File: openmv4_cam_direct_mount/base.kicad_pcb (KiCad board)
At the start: 4 copper layers, 35.6 x 44.5 mm, 59 parts, among them M1 9774030243R, M2 9774030243R, Q1 BSS138, Q2 Si2301BDS, U1 STM32H743VIT6, U5 TPS731XX, U8 PAM2305AABADJ, X1 MF-CON-MICROUSB-RIGHT, X2 USD-1040310811, X3 DF12-36-DS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

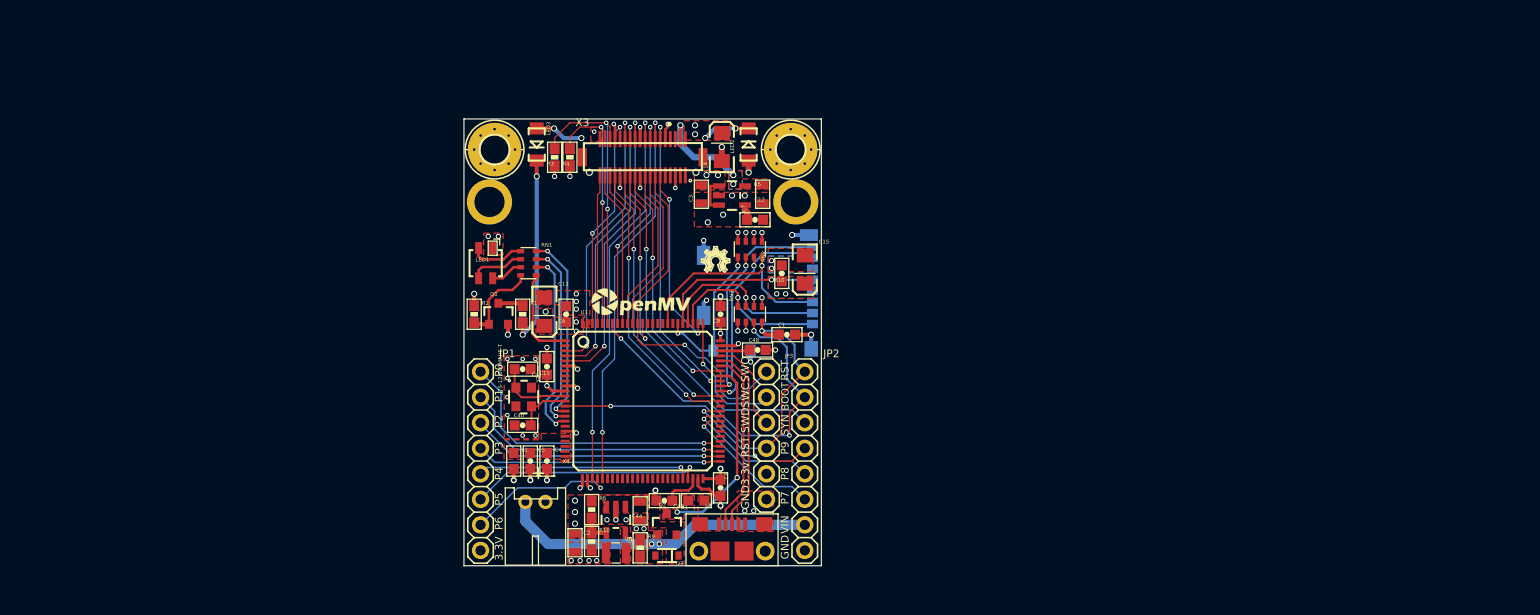
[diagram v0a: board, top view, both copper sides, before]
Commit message: Fixed camera mount hole links
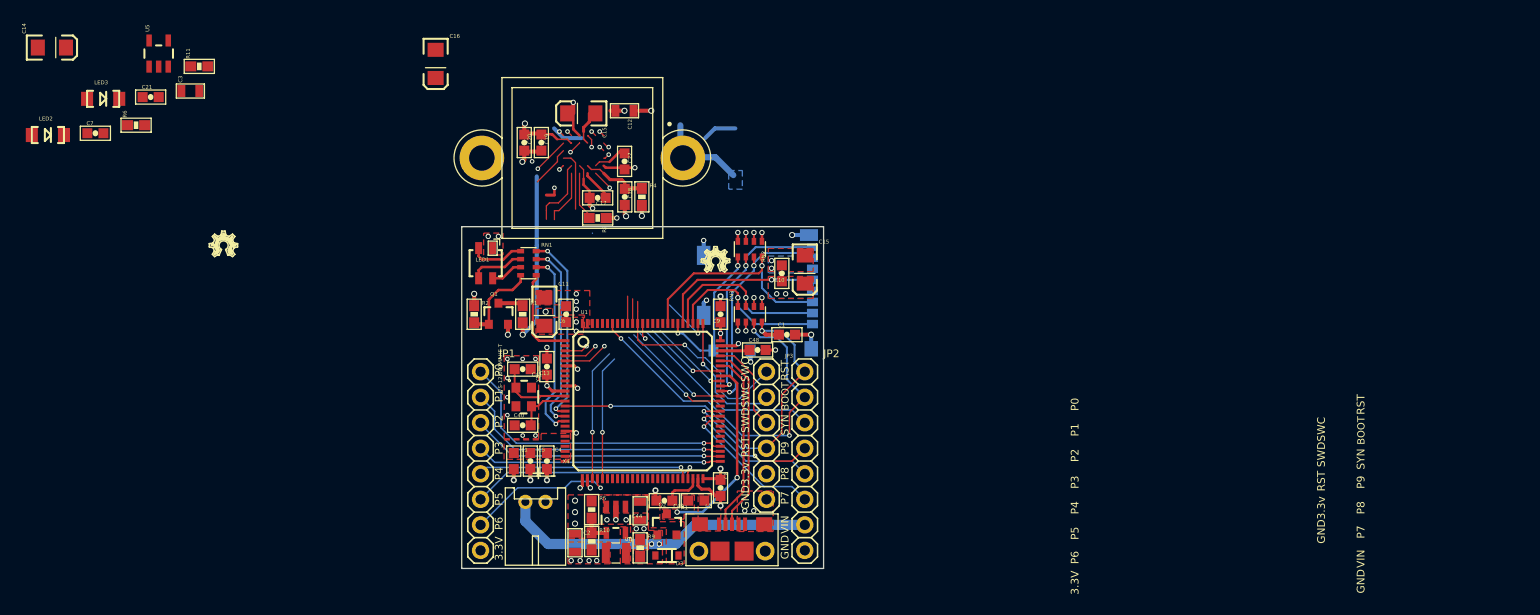
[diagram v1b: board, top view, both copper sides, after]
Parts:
- removed H1, H2: MOUNT-PAD-ROUND2.8, base:2,8-PAD
- removed M1, M2: 9774030243R, base:9774030151R
- removed U$1: , base:WEEE
- removed U$2: , base:ROHS
- removed U$4: , base:OMV-LOGO-SMALL
- removed X3: DF12-36-DS, base:DF12-36-DS
- added C15: 47uF, base:EIA3216, F.Cu at (142.4, 82.2)
- added C16: 47uF, base:EIA3216, F.Cu at (127.9, 77.3)
- added C17: 0.1uF, base:0603-CAP, F.Cu at (144.0, 90.6)
- added C18: 22uF, base:0603-CAP, F.Cu at (146.7, 90.5)
- added C19: 4.7uF, base:0603-CAP, F.Cu at (138.4, 85.1)
- added C20: 0.1uF, base:0603-CAP, F.Cu at (136.7, 85.1)
- added C21: 0.1uF, base:0603-CAP, F.Cu at (99.5, 80.6)
- added C22: 0.1uF, base:0603-CAP, F.Cu at (146.7, 87.0)
- added LM1: LENSMOUNT20MM, openmv3:LENSMOUNT-20MM, F.Cu at (142.5, 86.7)
- added LOGO1: OSHW_LOGO_FILLX0100-NT, base:OSHW_FILLX100_NOTEXT, F.Cu at (105.4, 96.5)
- added R11: 10K, base:0603-RES, F.Cu at (104.4, 77.5)
- added R6: 10K, base:0603-RES, F.Cu at (98.1, 83.4)
- U$3: footprint base:OMV-LOGO -> openmv3:OMV-LOGO
- moved LED2 69.7 mm to (89.3, 84.4), turned to 0 degrees
- moved C14 67.4 mm to (89.7, 75.7), turned to 0 degrees
- moved C7 66.2 mm to (94.0, 84.2)
- moved U5 58.8 mm to (100.3, 76.3), turned to 0 degrees
- moved U$3 52.2 mm to (103.2, 97.2)
- moved C3 51.9 mm to (103.5, 80.0), turned to 0 degrees
- moved LED3 43.4 mm to (94.8, 80.8), turned to 0 degrees
- moved C12 16.1 mm to (146.7, 82.0), turned to 180 degrees
- moved R4 8.17 mm to (148.4, 90.5), turned to 270 degrees
- moved R3 7.41 mm to (144.0, 92.6), turned to 180 degrees
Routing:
- net /DCMI_HSYNC: track 39.2 -> 13.7 mm
- net /DCMI_PCLK: track 39.2 -> 13.7 mm
- net /DCMI_D7: track 29.6 -> 5.13 mm
- net Net-(LED2-PadC): track 22.3 -> 0.00 mm, vias 4 -> 0
- net /DCMI_D4: track 27.8 -> 5.93 mm
- net /DCMI_D3: track 21.9 -> 0.58 mm
- net /DCMI_D6: track 27.8 -> 7.10 mm
- net /DCMI_CLK: track 29.5 -> 9.39 mm
- net /I2C1_SCL: track 28.6 -> 10.4 mm, vias 2 -> 0
- net /I2C1_SDA: track 25.6 -> 7.93 mm, vias 2 -> 1
- net /DCMI_D0: track 28.6 -> 12.3 mm
- net /DCMI_FSIN: track 35.8 -> 19.5 mm, vias 1 -> 0
- net /DCMI_VSYNC: track 22.1 -> 6.01 mm, vias 2 -> 0
- net /DCMI_D1: track 27.8 -> 11.7 mm
- net /DCMI_PWDN: track 18.7 -> 2.97 mm
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- removed copper zone on F.Cu, net VDDA
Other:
- board size 35.6 x 44.5 mm -> 36 x 34 mm
- board text added: "10/15/2016"
- board text added: "OV7725-M7"
- board text added: "OpenMV3 R1"

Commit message: Changes to KiCAD
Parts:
- added U2: OV7725, openmv3:CSP2-28, F.Cu at (142.6, 86.3)
- moved X4 43.1 mm to (118.5, 82.4), turned to 0 degrees
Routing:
- net /SPI2_MOSI: track 29.0 -> 0.00 mm, vias 1 -> 0
- net /SPI2_MISO: track 27.1 -> 0.00 mm, vias 1 -> 0
- net /SPI2_SCLK: track 25.3 -> 0.13 mm, vias 1 -> 0
- net /SPI2_NSS: track 24.5 -> 0.00 mm, vias 1 -> 0
- net /I2C2_SDA: track 23.3 -> 0.01 mm, vias 1 -> 0
- net /I2C2_SCL: track 21.4 -> 0.01 mm, vias 1 -> 0
- net /LED_R: track 19.1 -> 1.14 mm, vias 2 -> 0
- net /LED_G: track 18.8 -> 1.14 mm, vias 2 -> 0
- net /LED_B: track 18.8 -> 1.14 mm, vias 2 -> 0
- net Net-(LED3-PadC): track 17.5 -> 1.18 mm
- net /DAC: track 15.0 -> 1.04 mm, vias 1 -> 0
- net /NRST: track 40.6 -> 26.7 mm, vias 2 -> 1
- net /DCMI_PCLK: track 13.7 -> 0.00 mm, vias 2 -> 0
- net /DCMI_HSYNC: track 13.7 -> 0.67 mm, vias 2 -> 1
- net /BOOT0: track 37.6 -> 26.9 mm, vias 3 -> 2
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- removed copper zone on B.Cu, net VDDA

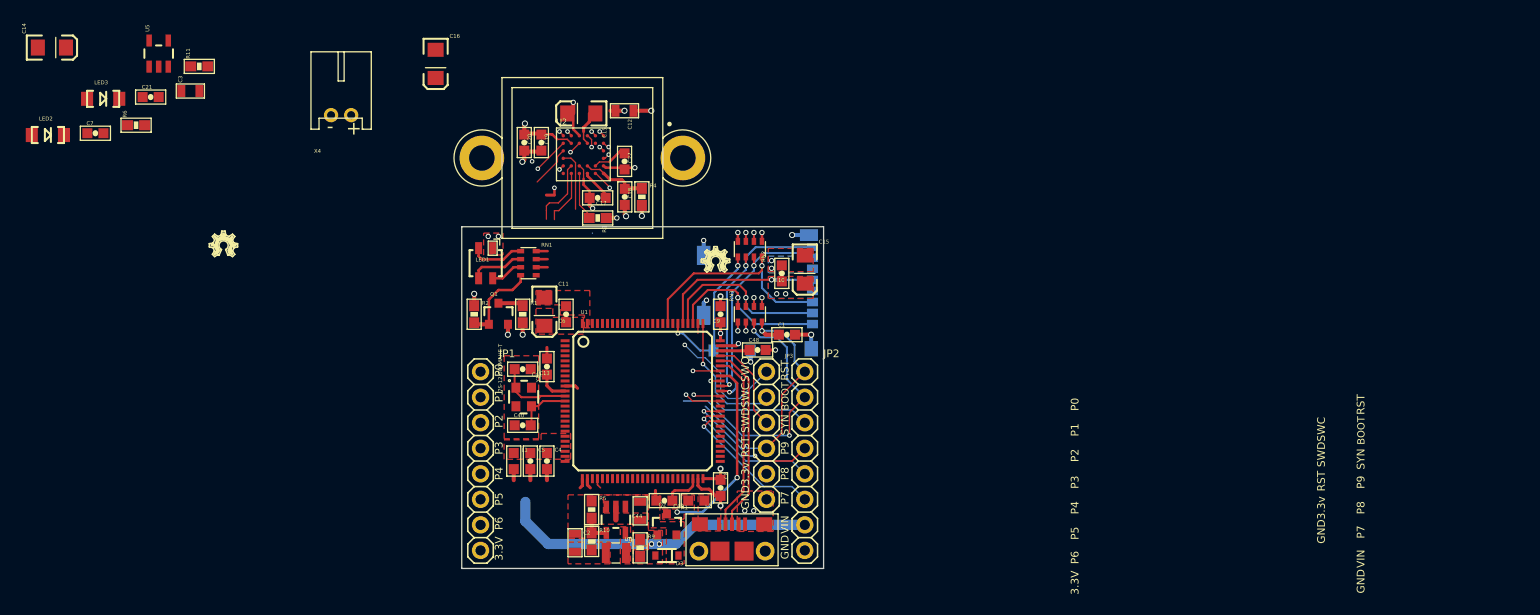
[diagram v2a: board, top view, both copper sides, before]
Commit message: Fixed cam position
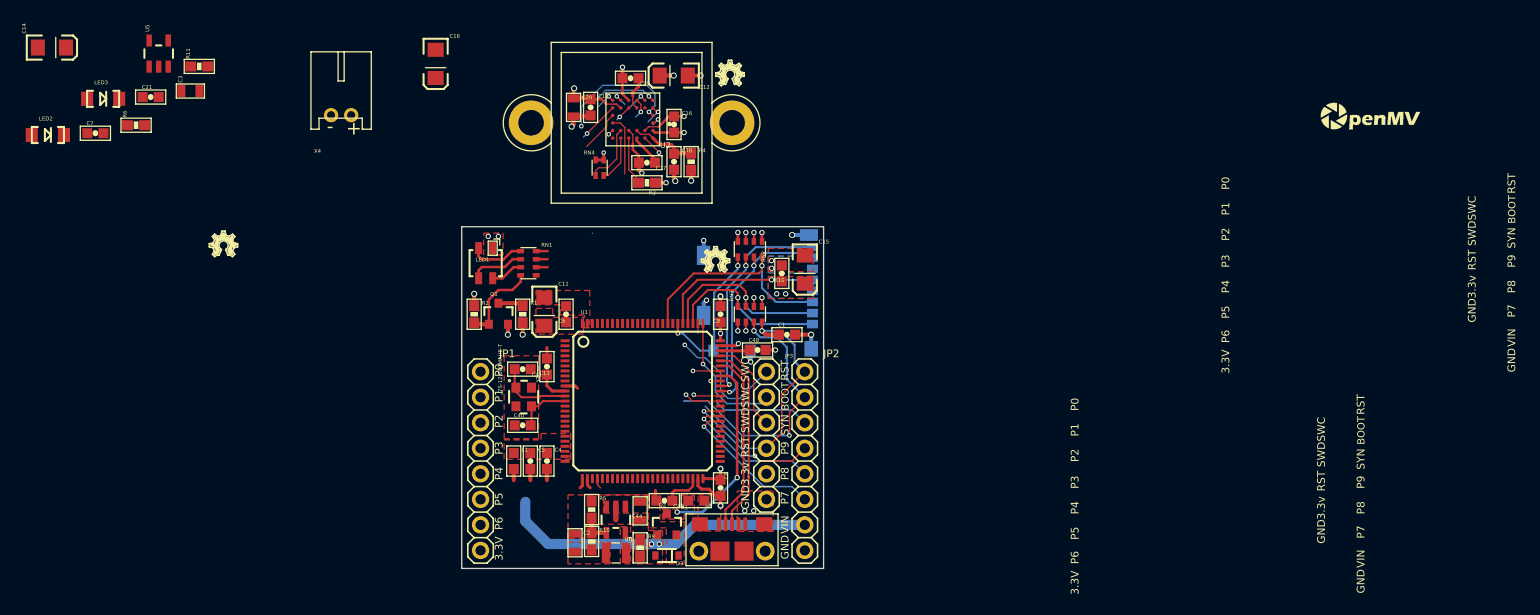
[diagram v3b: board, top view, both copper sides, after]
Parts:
- removed C22: 0.1uF, base:0603-CAP
- added C16: 0.1uF, openmv3:0603-CAP, F.Cu at (151.6, 83.3)
- added LOGO1: OSHW_LOGO_FILLX0100-NT, openmv3:OSHW_FILLX100_NOTEXT, F.Cu at (155.8, 79.5)
- added RN4: 4.7K, openmv3:EXBV4V, F.Cu at (144.2, 87.6)
- added U$1: , openmv3:WEEE, B.Cu at (218.5, 108.4)
- added U$2: , openmv3:ROHS, B.Cu at (212.8, 108.4)
- added U$3: , openmv3:OMV-LOGO, B.Cu at (227.0, 69.6)
- added U$4: , openmv3:OMV-LOGO-SMALL, F.Cu at (215.8, 84.0)
- C12: value 10uF -> 47uF; footprint base:0805 -> openmv3:EIA3216
- C15: value 47uF -> 0.1uF; footprint base:EIA3216 -> openmv3:0603-CAP
- C17: footprint base:0603-CAP -> openmv3:0603-CAP
- C18: value 22uF -> 4.7uF; footprint base:0603-CAP -> openmv3:0603-CAP
- C19: value 4.7uF -> 0.1uF; footprint base:0603-CAP -> openmv3:0603-CAP
- C20: value 0.1uF -> 22uF; footprint base:0603-CAP -> openmv3:0805
- R3: value 4.7K -> 10k; footprint base:0603-RES -> openmv3:0603-RES
- R4: value 4.7K -> 4.7R; footprint base:0603-RES -> openmv3:0603-RES
- moved U2 6.02 mm to (147.5, 82.8), turned to 180 degrees
- moved C17 6.02 mm to (148.9, 87.1)
- moved C18 6.02 mm to (151.6, 87.0)
- moved C19 6.02 mm to (143.3, 81.6)
- moved C20 6.02 mm to (141.6, 81.6)
- moved LM1 6.02 mm to (147.4, 83.2)
- moved R4 6.02 mm to (153.3, 87.0)
- moved C12 6.02 mm to (151.6, 78.5)
- moved C15 6.02 mm to (147.3, 78.7)
- moved R3 6.02 mm to (148.9, 89.1)
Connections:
- net Net-(LM1-PadP$1) renamed P$1
- net Net-(LM1-PadP$2) renamed P$2
- C17 pad 1: VCC -> Net-(C17-Pad1)
- C18 pad 1: VCC -> Net-(C18-Pad1)
- C19 pad 1: Net-(C19-Pad1) -> VCC
- C20 pad 1: Net-(C20-Pad1) -> VCC
- R3 pad 1: VCC -> GND
- R3 pad 2: /I2C1_SCL -> /FSIN
- R4 pad 1: VCC -> Net-(C18-Pad1)
- R4 pad 2: /I2C1_SDA -> VCC
- U2 pad A1: Net-(C19-Pad1) -> Net-(C18-Pad1)
- U2 pad A3: Net-(C21-Pad1) -> Net-(C17-Pad1)
- U2 pad A4: /DCMI_FSIN -> /FSIN
- U2 pad B3: Net-(C19-Pad1) -> Net-(C18-Pad1)
- U2 pad E3: Net-(C20-Pad1) -> Net-(C15-Pad1)
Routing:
- net VCC: track 38.4 -> 26.3 mm, vias 17 -> 16
- net /DCMI_D3: track 6.05 -> 13.2 mm, vias 1 -> 2
- net /DCMI_D7: track 0.00 -> 7.00 mm, vias 0 -> 1
- net Net-(U2-PadE2): track 6.89 -> 0.00 mm
- net Net-(C18-Pad1): track 0.00 -> 6.74 mm
- net /DCMI_VSYNC: track 0.54 -> 6.01 mm, vias 1 -> 0
- net /I2C1_SDA: track 1.05 -> 6.03 mm, vias 1 -> 0
- net /FSIN: track 0.00 -> 4.85 mm
- net /DCMI_D4: track 0.00 -> 4.10 mm, vias 0 -> 1
- net /DCMI_D1: track 8.26 -> 4.68 mm, vias 1 -> 2
- net /DCMI_D2: track 0.64 -> 4.21 mm, vias 1 -> 0
- net Net-(C15-Pad1): track 0.00 -> 3.35 mm
- net Net-(C17-Pad1): track 0.00 -> 3.20 mm
- net /DCMI_PWDN: track 4.21 -> 1.35 mm, vias 0 -> 1
- net GND: track 48.4 -> 46.1 mm, vias 22 -> 23
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
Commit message: Connecting key components
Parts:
- removed C14: 47uF, base:EIA3216
- removed the C15 at (164.6, 97.8)
- removed the C16 at (127.9, 77.3)
- removed JP1, JP2: PINHD-1X8, base:1X08
- removed LM1: LENSMOUNT20MM, openmv3:LENSMOUNT-20MM
- removed the LOGO1 at (155.8, 79.5)
- removed R11, R6: 10K, base:0603-RES
- removed RN4: 4.7K, openmv3:EXBV4V
- removed U$1: , openmv3:WEEE
- removed U$2: , openmv3:ROHS
- removed U$3 (x2): , openmv3:OMV-LOGO
- removed U$4: , openmv3:OMV-LOGO-SMALL
- removed X4: S2B-PH-K-S(LF)(SN), base:JST-PH-2-THM-RA
- added C22: 10uF, base:0805, F.Cu at (135.7, 127.6)
- added RN4A1: 4.7K, openmv3:EXBV4V, F.Cu at (145.2, 100.7)
- added RN4B1: 4.7K, openmv3:EXBV4V, F.Cu at (148.0, 100.7)
- C12, C15, C16, C17, C19, C20, U2: moved to B.Cu
- C18: footprint openmv3:0603-CAP -> base:0603-CAP; moved to B.Cu
- C21: value 0.1uF -> 47uF; footprint base:0603-CAP -> base:EIA3216
- R3: value 10k -> 10K; footprint openmv3:0603-RES -> base:0603-RES; moved to B.Cu
- R4: value 4.7R -> 10K; moved to B.Cu
- moved C21 68.0 mm to (165.3, 98.0), turned to 270 degrees
- moved U5 59.7 mm to (135.8, 124.3)
- moved LED2 55.2 mm to (143.0, 97.2), turned to 90 degrees
- moved C7 54.1 mm to (132.0, 122.8), turned to 90 degrees
- moved C3 52.4 mm to (135.8, 121.3), turned to 180 degrees
- moved LED3 48.9 mm to (140.9, 97.2), turned to 270 degrees
- moved C12 37.5 mm to (150.7, 115.9)
- moved C15 37.0 mm to (146.4, 115.7)
- moved C19 31.2 mm to (142.4, 112.8), turned to 90 degrees
- moved C20 31.2 mm to (140.7, 112.8), turned to 90 degrees
- moved U2 28.8 mm to (146.6, 111.6)
- moved C16 27.8 mm to (150.7, 111.1), turned to 90 degrees
- moved C18 20.4 mm to (150.7, 107.4), turned to 90 degrees
- moved R4 20.4 mm to (152.4, 107.4), turned to 90 degrees
- moved C17 20.2 mm to (148.0, 107.3)
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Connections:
- R3 pad 2: /FSIN -> /DCMI_FSIN
- U2 pad A4: /FSIN -> /DCMI_FSIN
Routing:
- net /LED_G: track 1.14 -> 19.4 mm, vias 0 -> 2
- net /LED_B: track 1.14 -> 19.4 mm, vias 0 -> 2
- net /LED_R: track 1.14 -> 19.3 mm, vias 0 -> 2
- net /DCMI_D3: track 13.2 -> 0.58 mm, vias 2 -> 3
- net /LED_IR: track 0.00 -> 9.76 mm, vias 0 -> 2
- net Net-(LED3-PadC): track 1.18 -> 8.82 mm, vias 2 -> 1
- net /DCMI_D7: track 7.00 -> 0.62 mm
- net /I2C1_SCL: track 4.68 -> 10.4 mm, vias 0 -> 1
- net /FSIN: track 4.85 -> 9.60 mm
- net /DCMI_FSIN: track 9.60 -> 4.85 mm
- net /DCMI_VSYNC: track 6.01 -> 9.11 mm, vias 0 -> 1
- net /DCMI_D2: track 4.21 -> 1.35 mm
- net /SPI3_SCLK/TRACESWO: track 12.5 -> 9.93 mm, vias 1 -> 0
- net /BOOT0: track 26.9 -> 24.5 mm, vias 2 -> 3
- net GND: track 46.1 -> 43.8 mm
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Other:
- net class 2 added: clearance 0.127, trace_width 0.25, via_dia 0.8, via_drill 0.4
- net class Default: trace_width 0.25 -> 0.127; via_dia 0.8 -> 0.457; via_drill 0.4 -> 0.254
- board text removed: "10/15/2016"
- board text removed: "10/27/18"
- board text removed: "OV7725-M7"
- board text removed: "OpenMV-H7 R1"
- board text removed: "OpenMV3 R1"
- board text removed: "P0=PB15/MOSI"
- board text removed: "P1=PB14/MISO"
- board text removed: "P2=PB13/SCLK"
- board text removed: "P3=PB12/SS"
- board text removed: "P4=PB10/TXD/SCL"
- board text removed: "P5=PB11/RXD/SDA"
- board text removed: "P6=PA5/ADC/DAC"
- board text removed: "P7=PD12/SERVO1"
- board text removed: "P8=PD13/SERVO2"
- board text removed: "P9=PD14/SERVO3"
- board text removed: "Pin List"
- board text removed: "https://openmv.io"

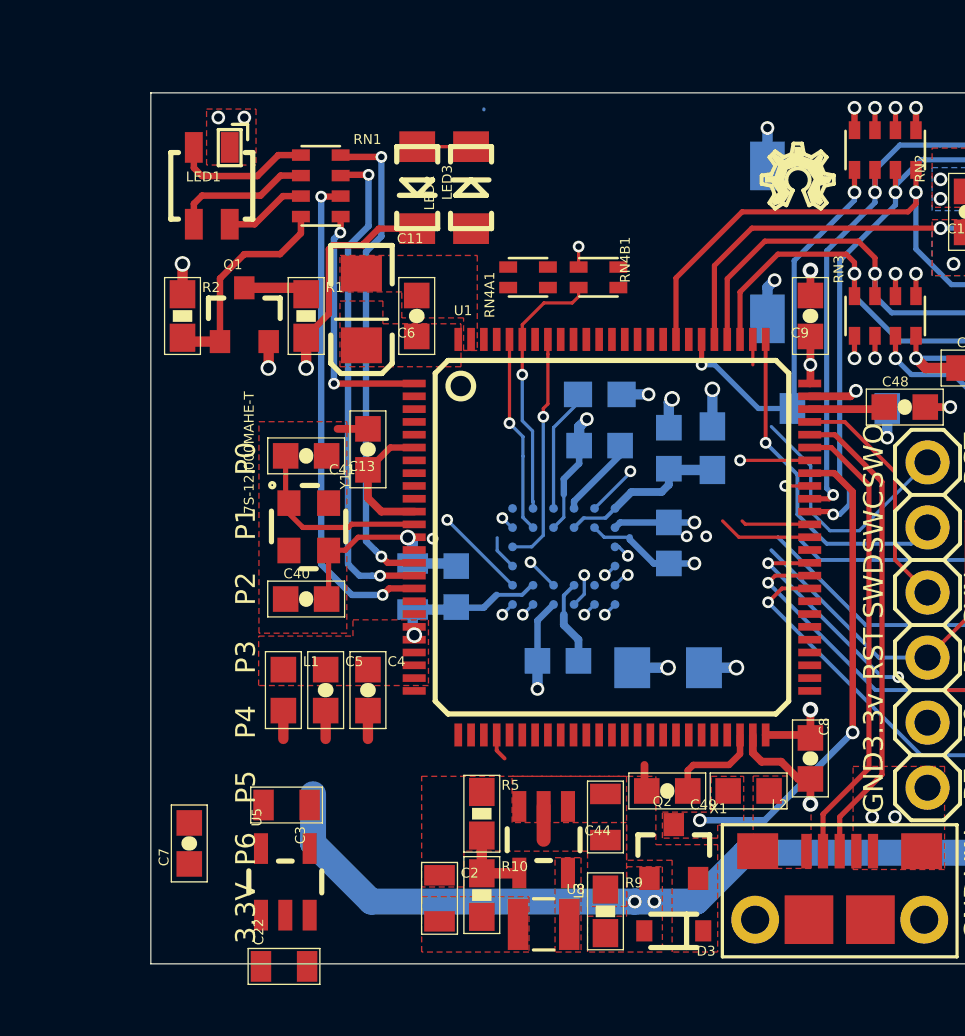
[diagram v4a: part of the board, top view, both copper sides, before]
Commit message: Connected LED's
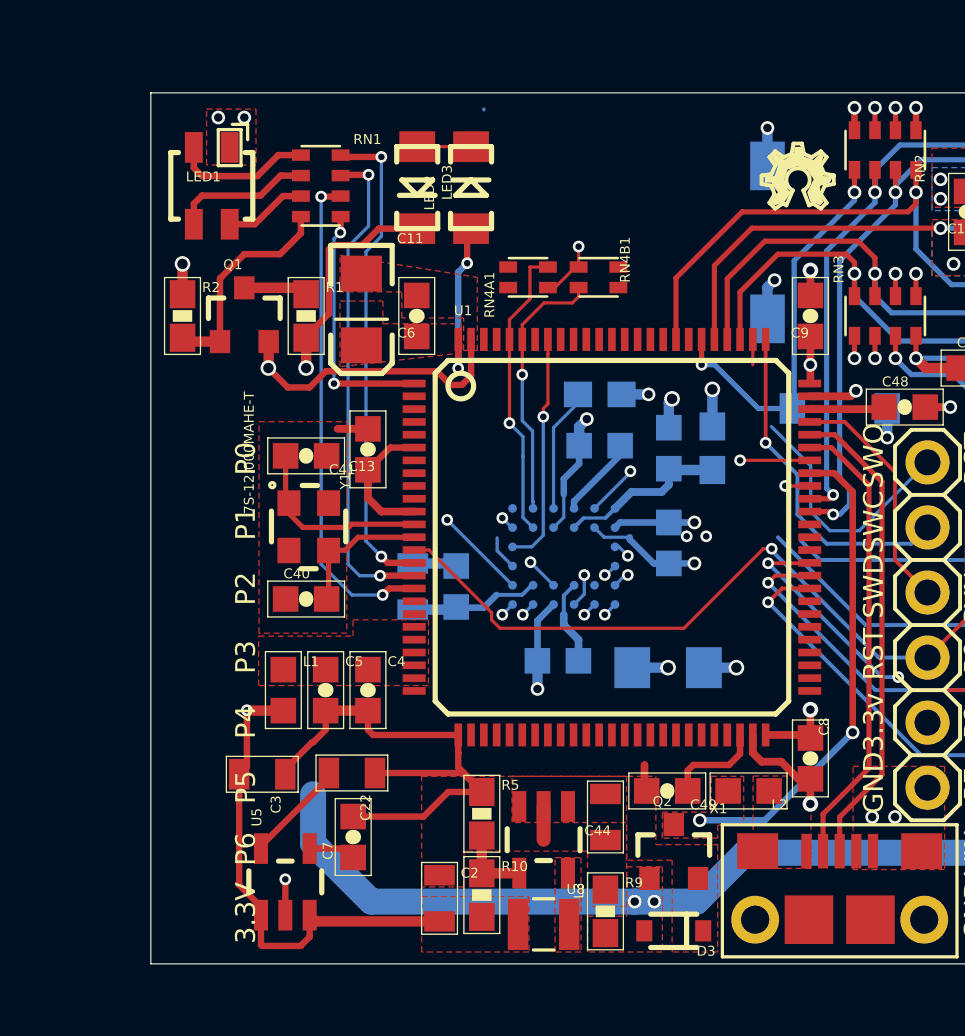
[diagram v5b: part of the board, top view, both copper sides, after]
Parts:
- moved C22 8.00 mm to (138.3, 120.0), turned to 180 degrees
- moved C7 6.40 mm to (138.4, 122.5)
- moved C3 1.53 mm to (134.8, 120.1)
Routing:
- net GND: track 43.8 -> 74.1 mm
- net VCC: track 26.7 -> 52.0 mm, vias 16 -> 18
- net /NRST: track 27.5 -> 44.2 mm, vias 2 -> 3
- net VDDA: track 0.00 -> 4.05 mm
- net /I2C1_SDA: track 7.73 -> 11.6 mm
- net /DCMI_D0: track 4.23 -> 0.57 mm
- net /DCMI_D1: track 3.26 -> 0.58 mm
- net Net-(C7-Pad1): track 0.00 -> 1.85 mm
- net /DAC: track 1.04 -> 0.00 mm
- net /DCMI_D3: vias 3 -> 2

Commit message: Made several connects
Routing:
- net Net-(X1-PadS1): track 0.00 -> 12.0 mm
- net /DCMI_D3: track 0.58 -> 11.7 mm
- net /DCMI_D6: track 0.57 -> 9.85 mm
- net /DCMI_D7: track 0.62 -> 9.74 mm
- net /DCMI_HSYNC: track 0.56 -> 9.42 mm, vias 1 -> 3
- net /DCMI_D2: track 1.35 -> 9.80 mm, vias 0 -> 1
- net VCC: track 52.0 -> 59.4 mm, vias 18 -> 20
- net /DCMI_D4: track 3.61 -> 8.80 mm
- net /NRST: track 44.2 -> 49.1 mm, vias 3 -> 5
- net GND: track 74.1 -> 74.2 mm, vias 23 -> 28
